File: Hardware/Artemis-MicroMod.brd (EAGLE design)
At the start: 22 x 22 mm, 29 parts, among them J2 MICROMOD-2222, U1 ARTEMIS_MODULESMD, U6 CH340E_MSOP10, Y1 32.768kHz

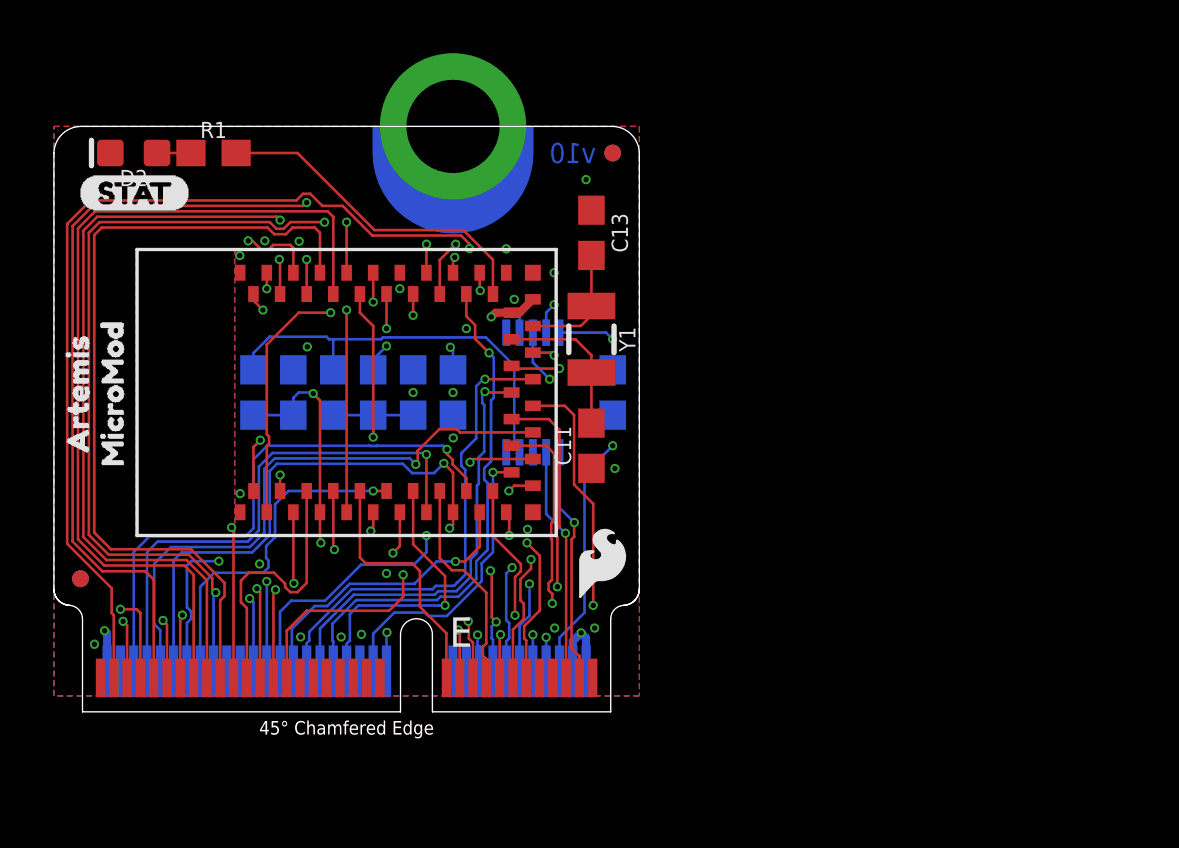
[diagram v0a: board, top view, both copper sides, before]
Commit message: v11 adds ADC buffers, 3.3V enable, RTC backup power, 0402 components.
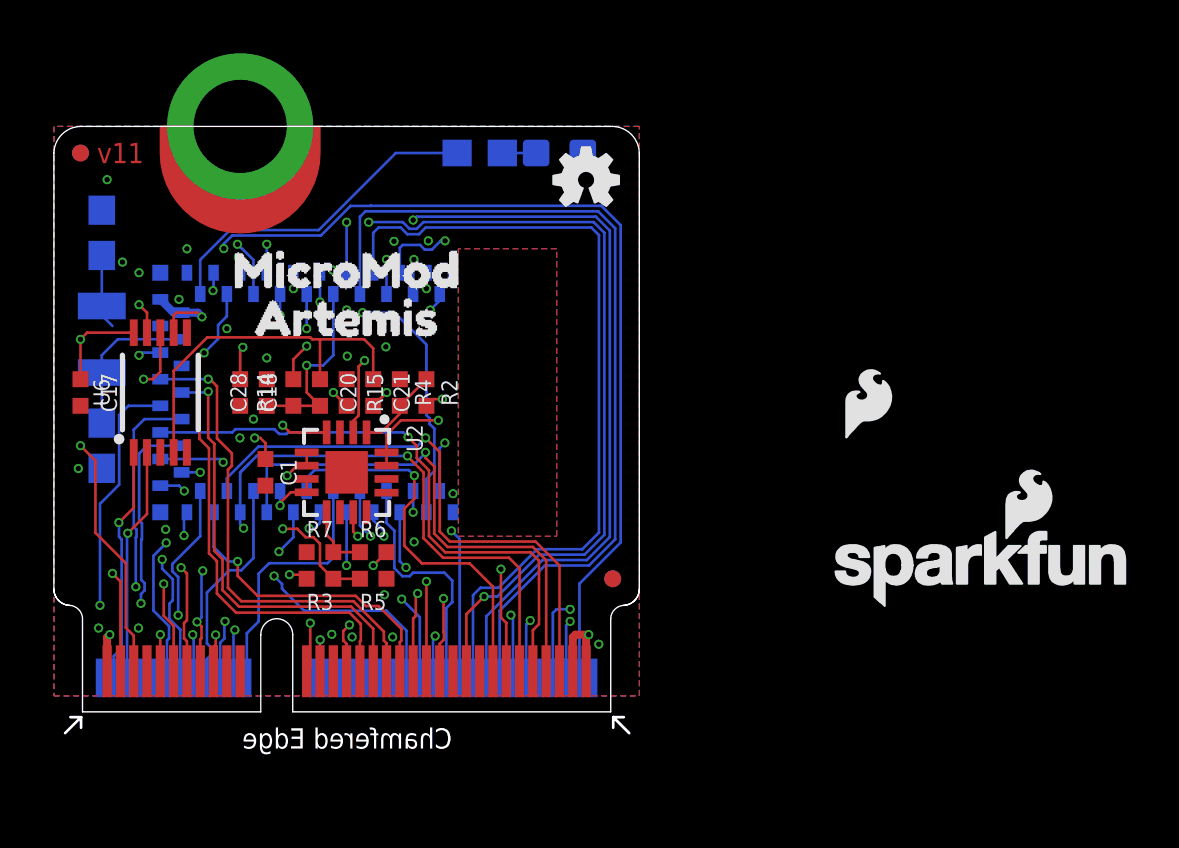
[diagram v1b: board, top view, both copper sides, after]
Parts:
- removed J2: MICROMOD-2222, Teensy:M.2-CARD-E-22
- added C1: 0.1uF, SparkFun-Capacitors:0402-TIGHT
- added J1: MICROMOD-2222, SparkFun-MicroMod:M.2-CARD-E-22
- added R2, R3, R6: 100k, SparkFun-Resistors:0402-TIGHT
- added R4, R5, R7: 150k, SparkFun-Resistors:0402-TIGHT
- added U2: TSV524, OpAmp:QFN-16
- C17, C18, C20, C21: device SparkFun-Capacitors:0603 -> SparkFun-Capacitors:0402-TIGHT
- C28: value 1nF -> 1.0nF; device SparkFun-Capacitors:0603 -> SparkFun-Capacitors:0402-TIGHT
- R14: device SparkFun-Resistors:0603 -> SparkFun-Resistors:0402-TIGHT
- R15: value 220k -> 220KOHM-0402T-1/16W-1%; device SparkFun-Resistors:0603 -> SparkFun-Resistors:0402-TIGHT
- moved FRAME1 40.2 mm to (31.1, -8.02), flipped to the bottom
- moved LOGO4 28.8 mm to (-3.40, 50.8), flipped to the bottom
- moved LOGO1 23.8 mm to (34.9, 5.40), flipped to the top
- moved U$3 21.0 mm to (20.9, 18.1), flipped to the bottom, turned to 0 degrees
- moved U$1 20.2 mm to (21.1, 19.5), flipped to the bottom
- moved C17 20.0 mm to (1.00, 12.0), flipped to the top
- moved FD1 20.0 mm to (21.0, 5.00), flipped to the bottom
- moved FD2 20.0 mm to (1.00, 21.0), flipped to the bottom
- moved FD3 20.0 mm to (1.00, 21.0), flipped to the top
- moved FD4 20.0 mm to (21.0, 5.00), flipped to the top
- moved C11 18.4 mm to (1.80, 10.0), flipped to the bottom
- moved C13 18.4 mm to (1.80, 18.0), flipped to the bottom
- moved Y1 18.4 mm to (1.80, 14.0), flipped to the bottom
- moved LOGO3 18.0 mm to (20.0, 20.0), flipped to the top
- moved U$2 16.8 mm to (15.0, 18.1), flipped to the bottom, turned to 0 degrees
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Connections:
- removed net GPIO11: J2.8, U1.~AD11
- removed net GPIO8: J2.67, U1.D3
- removed net N$8: C13.2, U1.XI, Y1.P$1
- removed net RTS0: J2.13, U1.D10
- removed net RX0: J2.19, U1.~D25
- removed net TX0: J2.17, U1.~D24
- new net 3.3V_EN: J1.4, U1.D3
- new net CAM_PCLK: J1.54, U1.~AD11
- new net N$10: R2.1, R4.2, U2.1
- new net N$3: R6.1, R7.2, U2.9
- new net N$4: U1.XI
- new net N$5: C13.2, Y1.P$1
- new net N$9: R3.1, R5.2, U2.4
- new net RTS1: J1.13, U1.D10
- new net RX1: J1.19, U1.~D25
- new net SCALED_ADC0: U1.~AD32, U2.5, U2.6
- new net SCALED_ADC1: U1.~AD35, U2.7, U2.8
- new net SCALED_BATT_VIN/3: U1.~AD31, U2.15, U2.16
- new net TX1: J1.17, U1.~D24
- net !RESET!: now also J1.6; no longer J2.6
- net 3.3V: now also C1.1, J1.2, J1.72, J1.74, U2.2; no longer J2.2, J2.4, J2.74
- net ADC0: now also J1.34, R3.2; no longer J2.34, U1.~AD32
- net ADC1: now also J1.38, R6.2; no longer J2.38, U1.~AD35
- net ADC_D+: now also J1.63; no longer J2.63
- net ADC_D-: now also J1.65; no longer J2.65
- net BATT_VIN/3: now also J1.51, R2.2; no longer J2.51, U1.~AD31
- net BOOT: now also J1.11; no longer J2.11
- net CLKOUT: now also J1.56; no longer J2.58
- net CTS1: now also J1.15; no longer J2.15
- net D0: now also J1.10; no longer J2.10
- net D1: now also J1.18; no longer J2.18
- net GND: now also C1.2, J1.1, J1.33, J1.36, J1.39, J1.45, J1.7, J1.75, J1.GND, J1.GND-SM-B, R4.1, R5.1, R7.1, U2.11; no longer J2.1, J2.33, J2.36, J2.39, J2.45, J2.7, J2.75, J2.GND, J2.GND-SM-B
- net GPIO0: now also J1.40; no longer J2.40
- net GPIO1: now also J1.42; no longer J2.42
- net GPIO2: now also J1.44; no longer J2.44
- net GPIO3: now also J1.46; no longer J2.46
- net GPIO4: now also J1.48; no longer J2.48
- net GPIO5: now also J1.73; no longer J2.73
- net GPIO6: now also J1.71; no longer J2.71
- net GPIO7: now also J1.69; no longer J2.69
- net I2C_!INT!: now also J1.16; no longer J2.16
- net PDM_CLK: now also J1.50; no longer J2.50
- net PDM_DATA: now also J1.52; no longer J2.52
- net PWM0: now also J1.32; no longer J2.32
- net PWM1: now also J1.47; no longer J2.47
- net SCL: now also J1.14; no longer J2.14
- net SCL1: now also J1.55; no longer J2.55
- net SDA: now also J1.12; no longer J2.12
- net SDA1: now also J1.53; no longer J2.53
- net SDIO_DATA0: now also J1.64; no longer J2.64
- net SDIO_DATA1: now also J1.66; no longer J2.66
- net SDIO_DATA2: now also J1.68; no longer J2.68
- net SDIO_DATA3: now also J1.70; no longer J2.70
- net SPI_!CS!: now also J1.49; no longer J2.49
- net SPI_MISO: now also J1.61; no longer J2.61
- net SPI_MOSI: now also J1.59; no longer J2.59
- net SPI_MOSI1: now also J1.62; no longer J2.62
- net SPI_SCK: now also J1.57; no longer J2.57
- net SPI_SCK1: now also J1.60; no longer J2.60
- net SWDCK: now also J1.21; no longer J2.21
- net SWDIO: now also J1.23; no longer J2.23
- net USB_D+: now also J1.3; no longer J2.3
- net USB_D-: now also J1.5; no longer J2.5
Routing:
- net GPIO8: track 31.8 -> 0.00 mm, vias 2 -> 0
- net 3.3V_EN: track 0.00 -> 27.1 mm, vias 0 -> 3
- net SCALED_BATT_VIN/3: track 0.00 -> 20.2 mm, vias 0 -> 3
- net RTS1: track 0.00 -> 15.3 mm, vias 0 -> 2
- net BATT_VIN/3: track 26.7 -> 11.5 mm, vias 3 -> 2
- net RTS0: track 14.8 -> 0.00 mm, vias 2 -> 0
- net GPIO11: track 13.5 -> 0.00 mm, vias 2 -> 0
- net RX1: track 0.00 -> 10.7 mm, vias 0 -> 2
- net RX0: track 10.6 -> 0.00 mm, vias 2 -> 0
- net N$9: track 0.00 -> 10.3 mm, vias 0 -> 2
- net TX1: track 0.00 -> 8.14 mm
- net TX0: track 8.14 -> 0.00 mm
- net ADC0: track 11.4 -> 4.95 mm, vias 1 -> 2
- net ADC1: track 10.7 -> 5.20 mm, vias 1 -> 2
- net SCALED_ADC0: track 0.00 -> 5.40 mm, vias 0 -> 2
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- added copper zone on layer 15, net 3.3V
- removed copper zone on layer 2, net 3.3V
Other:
- outline, holes or cut-outs redrawn
- board text added: "0.8mm PCB 45 degree chamfered edge Four layer design"
- board text added: "v11"
- board text removed: "0.8mm PCB 45 degree chamfered edge"
- board text removed: "45° Chamfered Edge"
- board text removed: "v10"

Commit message: Routed CAM_PCLK
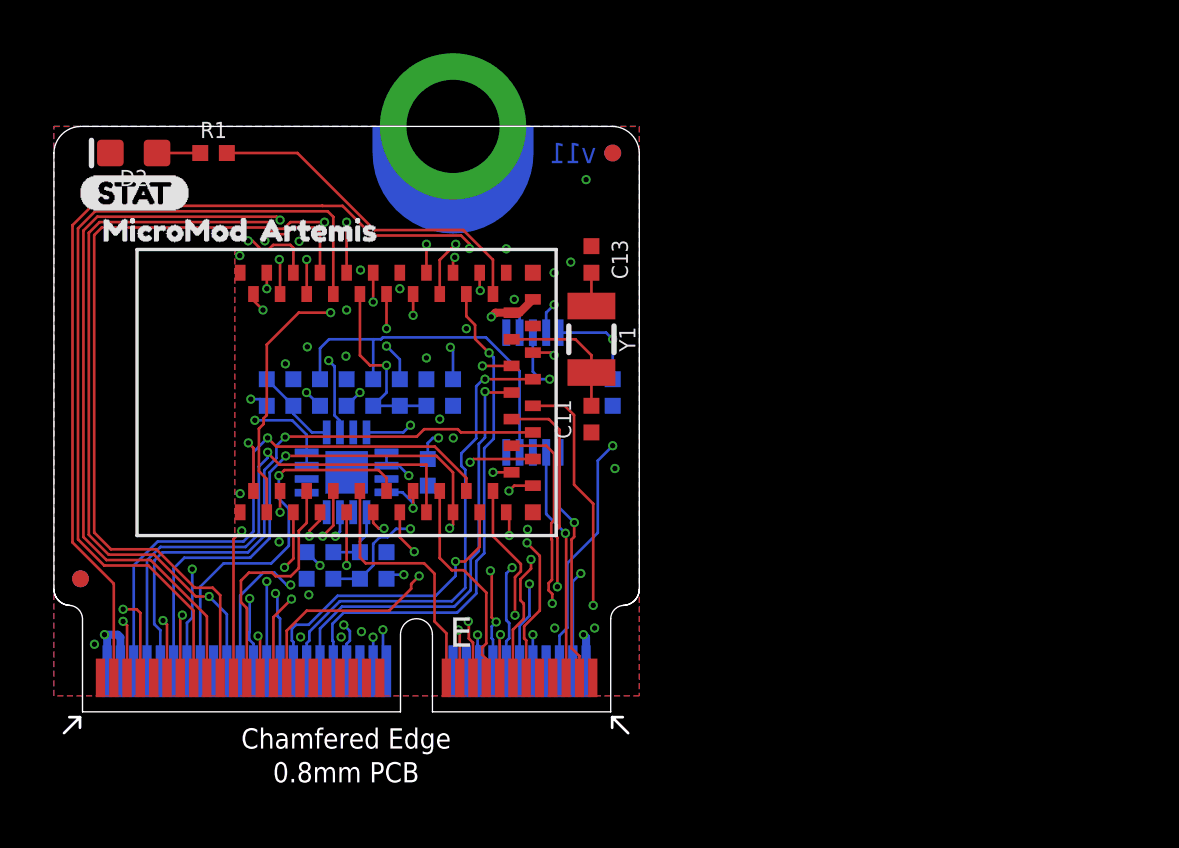
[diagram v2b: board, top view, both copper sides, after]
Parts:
- removed LOGO2: SFE_LOGO_FLAME.1_INCH, SparkFun-Aesthetics:SFE_LOGO_FLAME_.1
- C11, C13: device SparkFun-Capacitors:0603 -> SparkFun-Capacitors:0402-TIGHT
- R1: device SparkFun-Resistors:0603 -> SparkFun-Resistors:0402-TIGHT
- moved FRAME1 40.2 mm to (-9.11, -8.02), flipped to the top
- moved LOGO4 28.8 mm to (25.4, 50.8), flipped to the top
- moved LOGO1 26.6 mm to (11.0, 17.0), flipped to the bottom
- moved U$1 20.2 mm to (0.90, 19.5), flipped to the top
- moved C17 20.0 mm to (21.0, 12.0), flipped to the bottom
- moved FD1 20.0 mm to (1.00, 5.00), flipped to the top
- moved FD2 20.0 mm to (21.0, 21.0), flipped to the top
- moved FD3 20.0 mm to (21.0, 21.0), flipped to the bottom
- moved FD4 20.0 mm to (1.00, 5.00), flipped to the bottom
- moved U$3 19.8 mm to (1.10, 18.1), flipped to the top
- moved C11 18.4 mm to (20.2, 11.0), flipped to the top
- moved C13 18.4 mm to (20.2, 17.0), flipped to the top
- moved Y1 18.4 mm to (20.2, 14.0), flipped to the top
- moved LOGO3 18.0 mm to (2.00, 20.0), flipped to the bottom
- moved D2 16.0 mm to (3.00, 21.0), flipped to the top
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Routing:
- net CAM_PCLK: track 0.00 -> 22.7 mm, vias 0 -> 3
- net N$5: track 2.82 -> 1.60 mm
- net N$7: track 5.80 -> 5.15 mm
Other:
- outline, holes or cut-outs redrawn

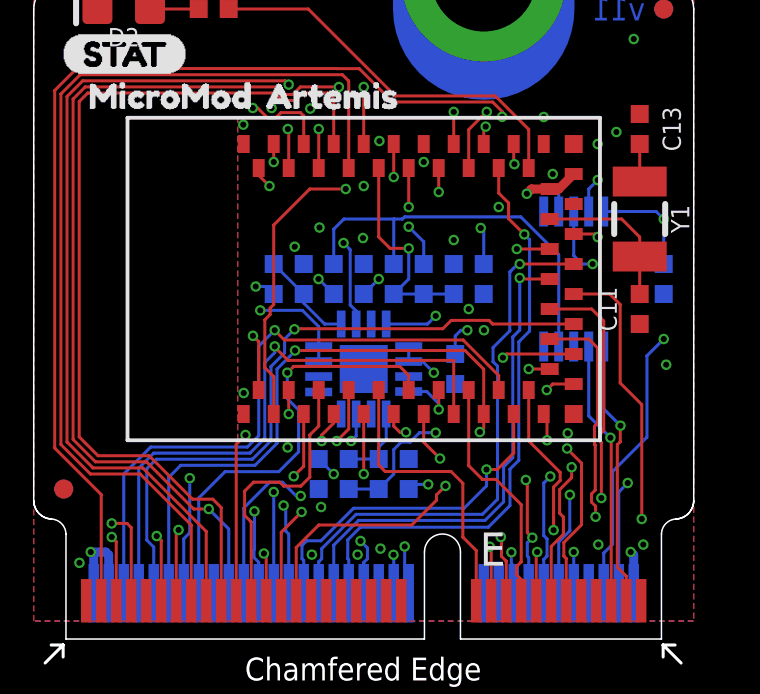
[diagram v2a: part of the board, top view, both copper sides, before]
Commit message: Double buffered ADC.
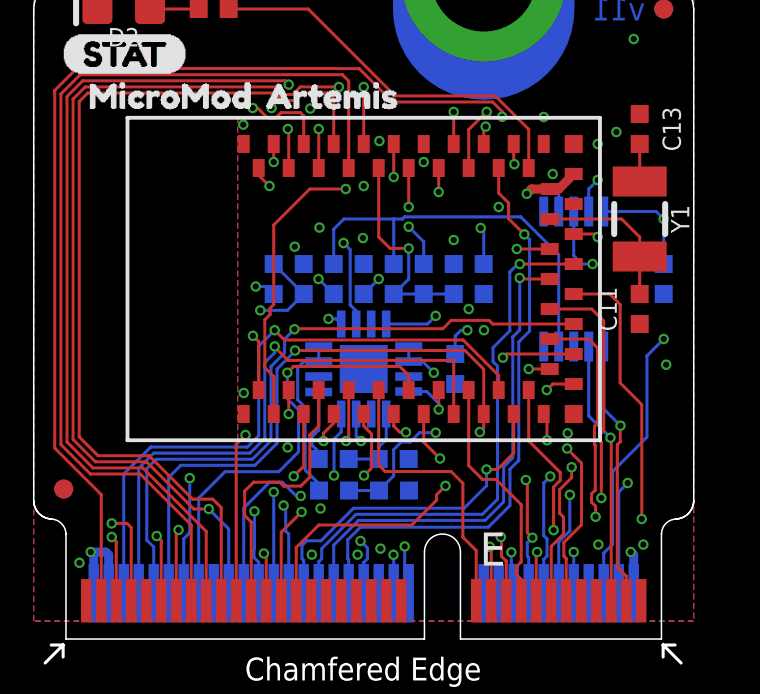
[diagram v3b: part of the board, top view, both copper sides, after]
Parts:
- moved R5 2.01 mm to (12.0, 4.95), turned to 0 degrees
- moved R3 1.99 mm to (10.0, 4.95), turned to 0 degrees
- moved FRAME1 0.86 mm to (-9.97, -8.02)
- moved LOGO4 0.86 mm to (24.5, 50.8)
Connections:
- net N$3 renamed ADC1_BUFF2
- net N$9 renamed ADC0_BUFF2
- removed net N$10: R2.1, R4.2, U2.1
- new net ADC0_BUFF1: R3.2, U2.15, U2.16
- new net ADC_BUFF1: R6.2, U2.13, U2.14
- net ADC0: now also U2.1; no longer R3.2
- net ADC1: now also U2.12; no longer R6.2
- net SCALED_BATT_VIN/3: now also R2.1, R4.2; no longer U2.15, U2.16
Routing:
- net ADC0_BUFF1: track 0.00 -> 5.67 mm
- net ADC0: track 5.30 -> 10.6 mm
- net N$10: track 3.25 -> 0.00 mm
- net ADC_BUFF1: track 0.00 -> 2.94 mm
- net ADC1: track 5.20 -> 6.59 mm

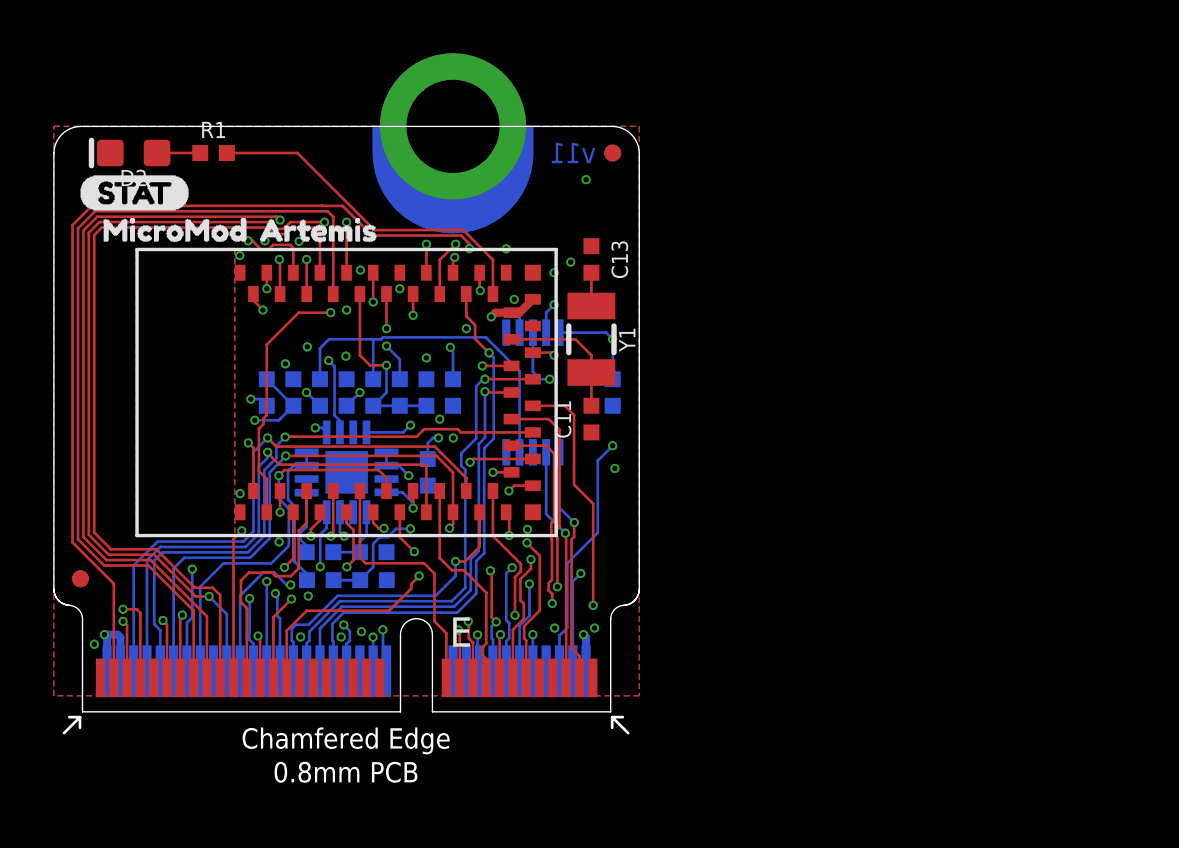
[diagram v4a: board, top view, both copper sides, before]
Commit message: Add reverse diode to prevent RTC 3.3V from driving 3.3V bus. Add test sketches.
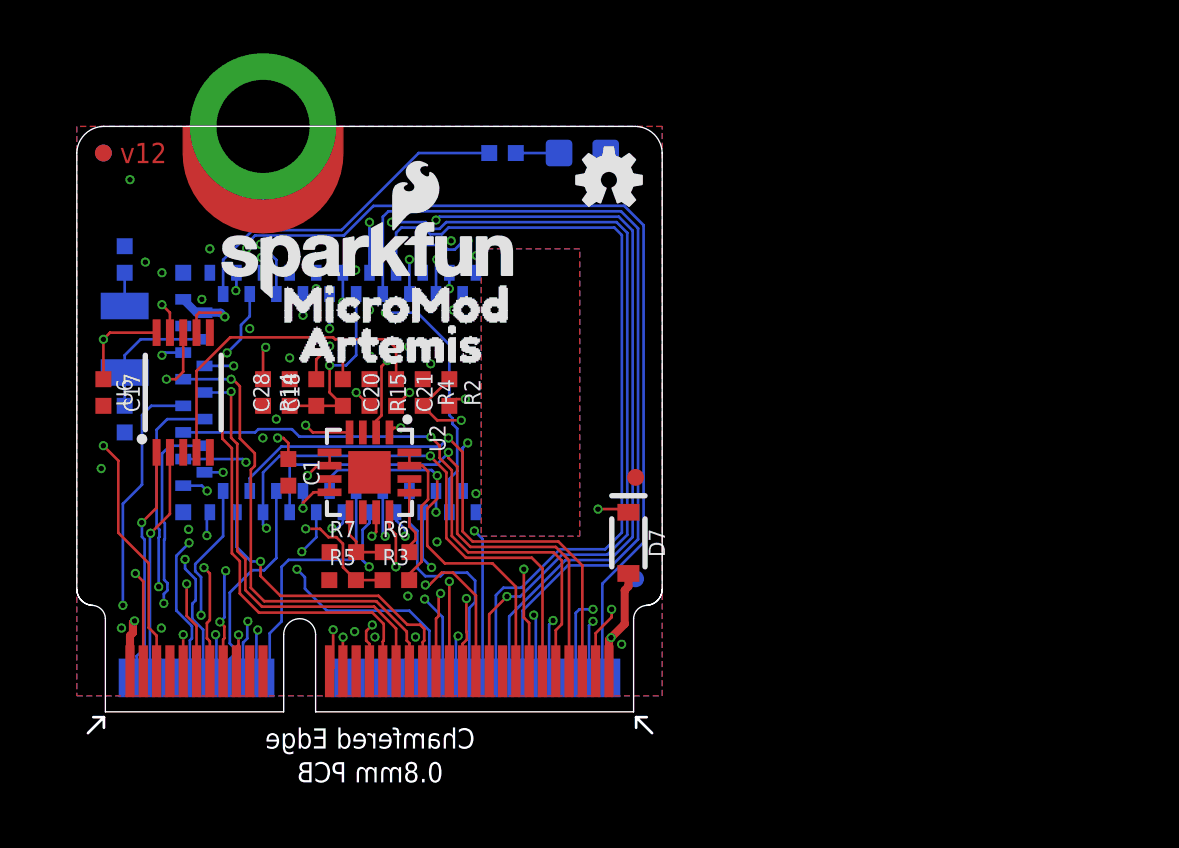
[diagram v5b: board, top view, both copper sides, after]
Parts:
- added D7: 1A/23V/620mV, SparkFun-DiscreteSemi:SOD-323
- moved FRAME1 42.8 mm to (32.8, -8.02), flipped to the bottom
- moved LOGO4 26.2 mm to (-1.68, 50.8), flipped to the bottom
- moved FD4 21.2 mm to (21.9, 8.81), flipped to the top
- moved U$1 21.1 mm to (22.0, 19.5), flipped to the bottom
- moved FD1 20.9 mm to (21.9, 5.00), flipped to the bottom
- moved U$3 20.7 mm to (21.8, 18.1), flipped to the bottom
- moved C17 19.1 mm to (1.86, 12.0), flipped to the top
- moved FD2 19.1 mm to (1.86, 21.0), flipped to the bottom
- moved FD3 19.1 mm to (1.86, 21.0), flipped to the top
- moved LOGO3 18.9 mm to (20.9, 20.0), flipped to the top
- moved C11 17.5 mm to (2.66, 11.0), flipped to the bottom
- moved C13 17.5 mm to (2.66, 17.0), flipped to the bottom
- moved Y1 17.5 mm to (2.66, 14.0), flipped to the bottom
- moved D2 16.9 mm to (19.9, 21.0), flipped to the bottom
- moved U6 13.1 mm to (4.86, 12.0), flipped to the top
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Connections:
- new net 3.3V_MAIN: D7.A, J1.2, J1.74
- net 3.3V: now also D7.C; no longer J1.2, J1.74
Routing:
- net 3.3V_MAIN: track 0.00 -> 27.5 mm, vias 0 -> 2
- net 3.3V: track 18.7 -> 17.7 mm
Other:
- outline, holes or cut-outs redrawn
- board text added: "v12"
- board text removed: "v11"
